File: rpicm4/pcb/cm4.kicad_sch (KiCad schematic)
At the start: 17 parts, among them J1 USB_C_Receptacle_USB2.0, J11 Conn_01x04_Male, J12 Conn_01x04_Male, J16 Conn_01x04_Male, J2 USB_C_Receptacle_USB2.0, J3 Conn_01x02_Male, J4 Conn_01x02_Male, J5 Conn_01x02_Male, J6 Conn_01x02_Male, J7 Conn_01x02_Male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

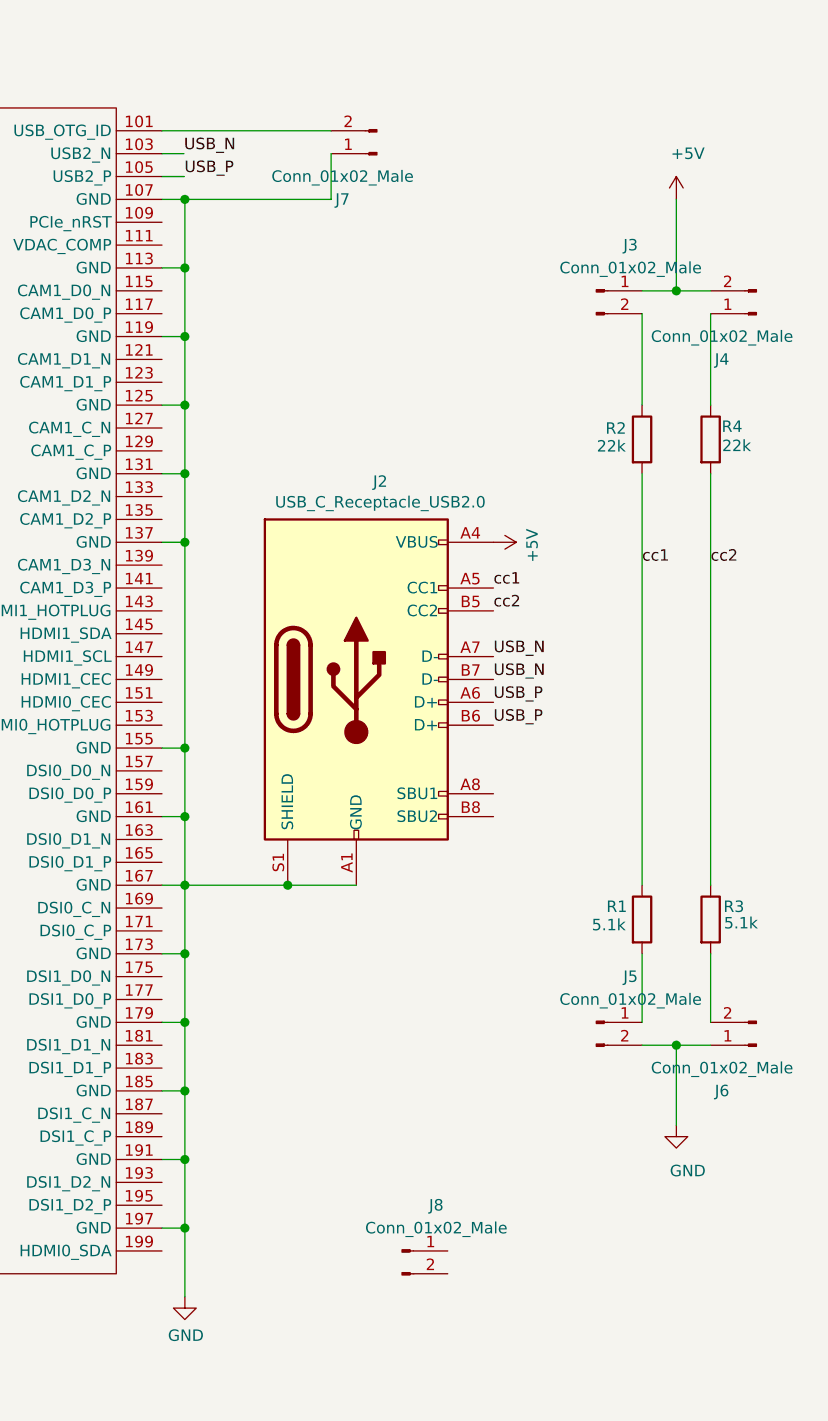
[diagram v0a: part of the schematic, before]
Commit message: rpicm4: better wiring
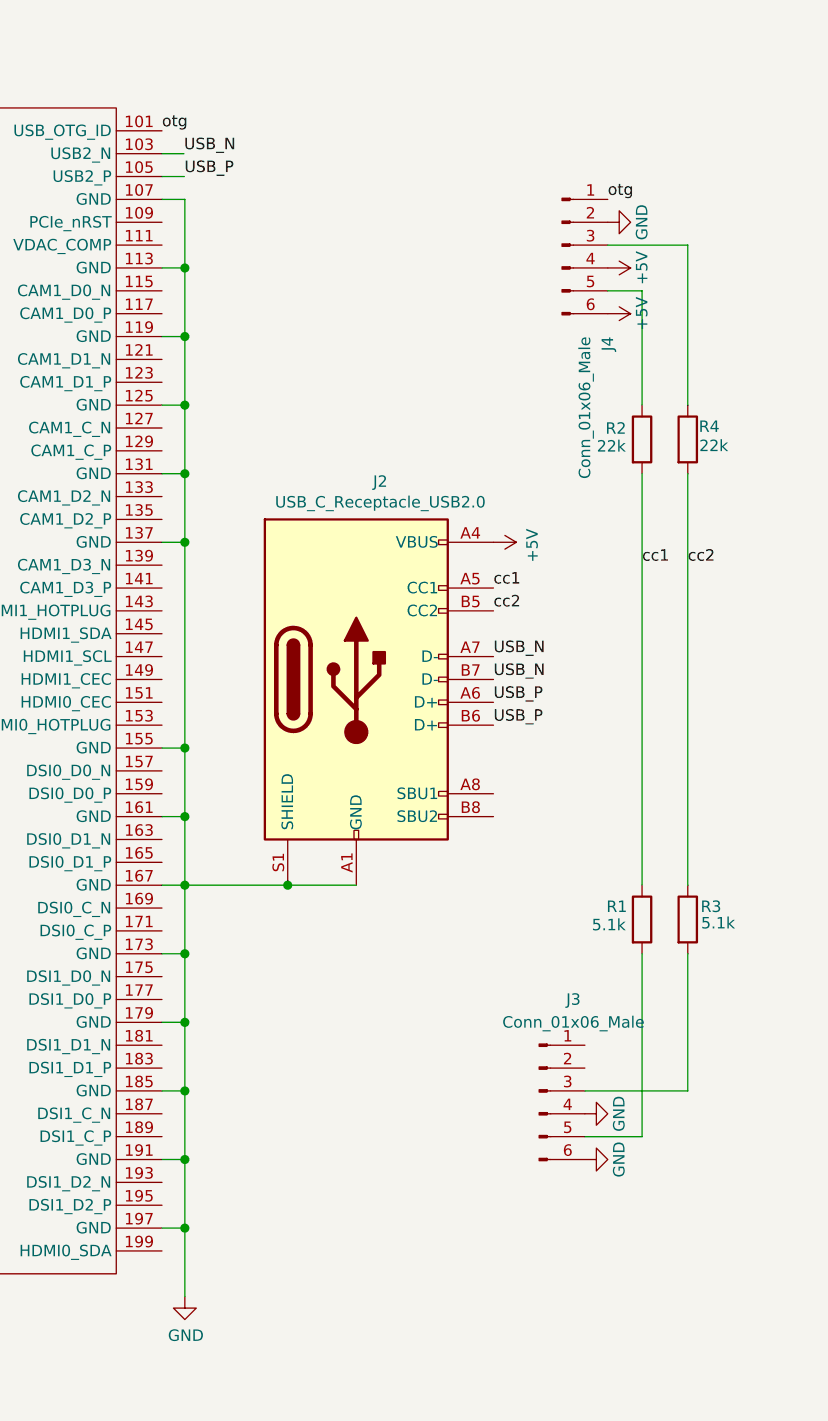
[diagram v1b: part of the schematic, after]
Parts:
- removed J3, J4, J5, J6, J7, J8: Conn_01x02_Male, Connector_PinHeader_2.54mm:PinHeader_1x02_P2.54mm_Vertical, symbol Connector:Conn_01x02_Male
- added J3, J4: Conn_01x06_Male, Connector_PinHeader_2.54mm:PinHeader_1x06_P2.54mm_Vertical, symbol Connector:Conn_01x06_Male
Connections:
- net +5V: now also J4.4 (Pin_4), J4.6 (Pin_6)
- net GND: now also J3.4 (Pin_4), J3.6 (Pin_6), J4.2 (Pin_2)
- net otg: now reaches Module1.101 (USB_OTG_ID)
- net otg: now also J4.1 (Pin_1)
- net at R3.2: now also J3.3 (Pin_3)
- net at R2.1: now also J4.5 (Pin_5)
- net at R4.1: now also J4.3 (Pin_3)
- net at R1.2: now also J3.5 (Pin_5)
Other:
- moved on the sheet: R3, R4
